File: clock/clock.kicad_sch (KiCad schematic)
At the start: 32 parts

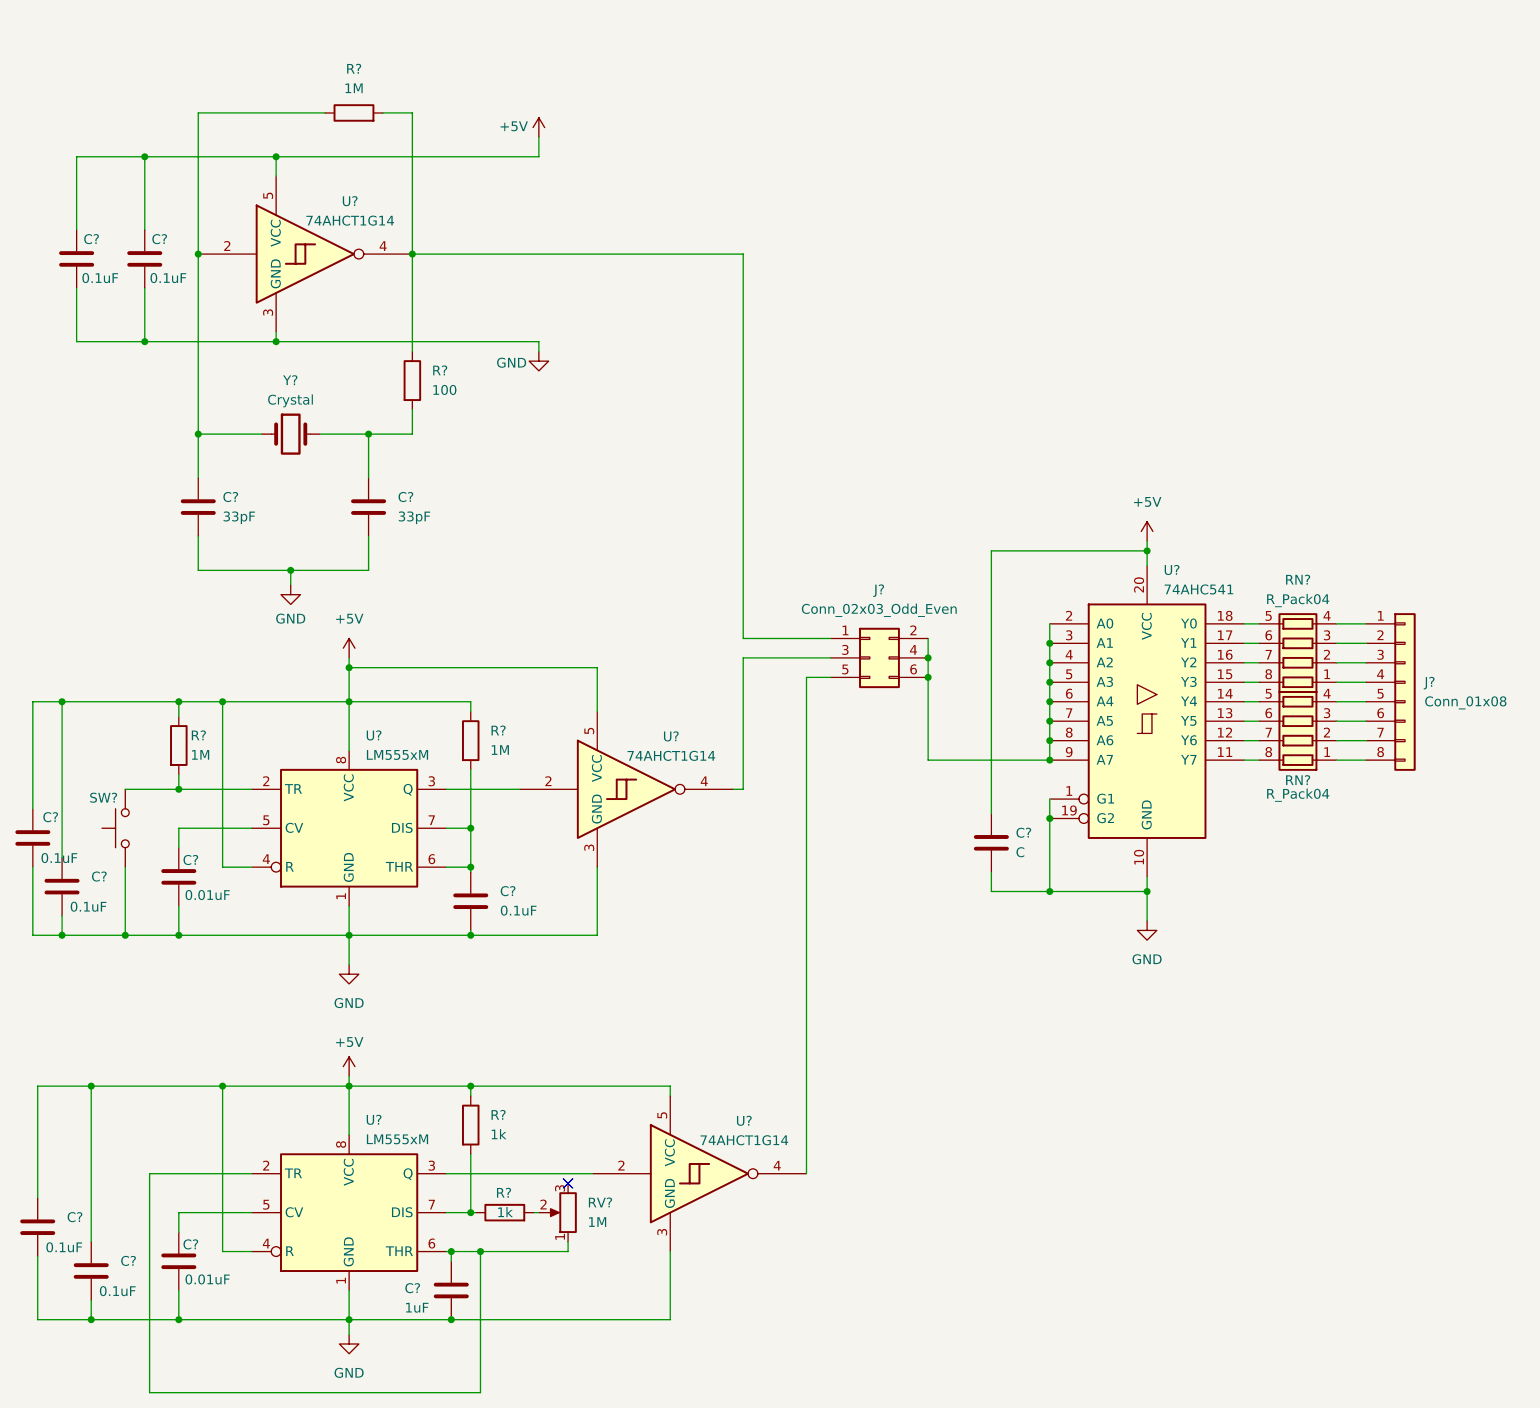
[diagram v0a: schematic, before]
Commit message: Finalized clock for fabrication
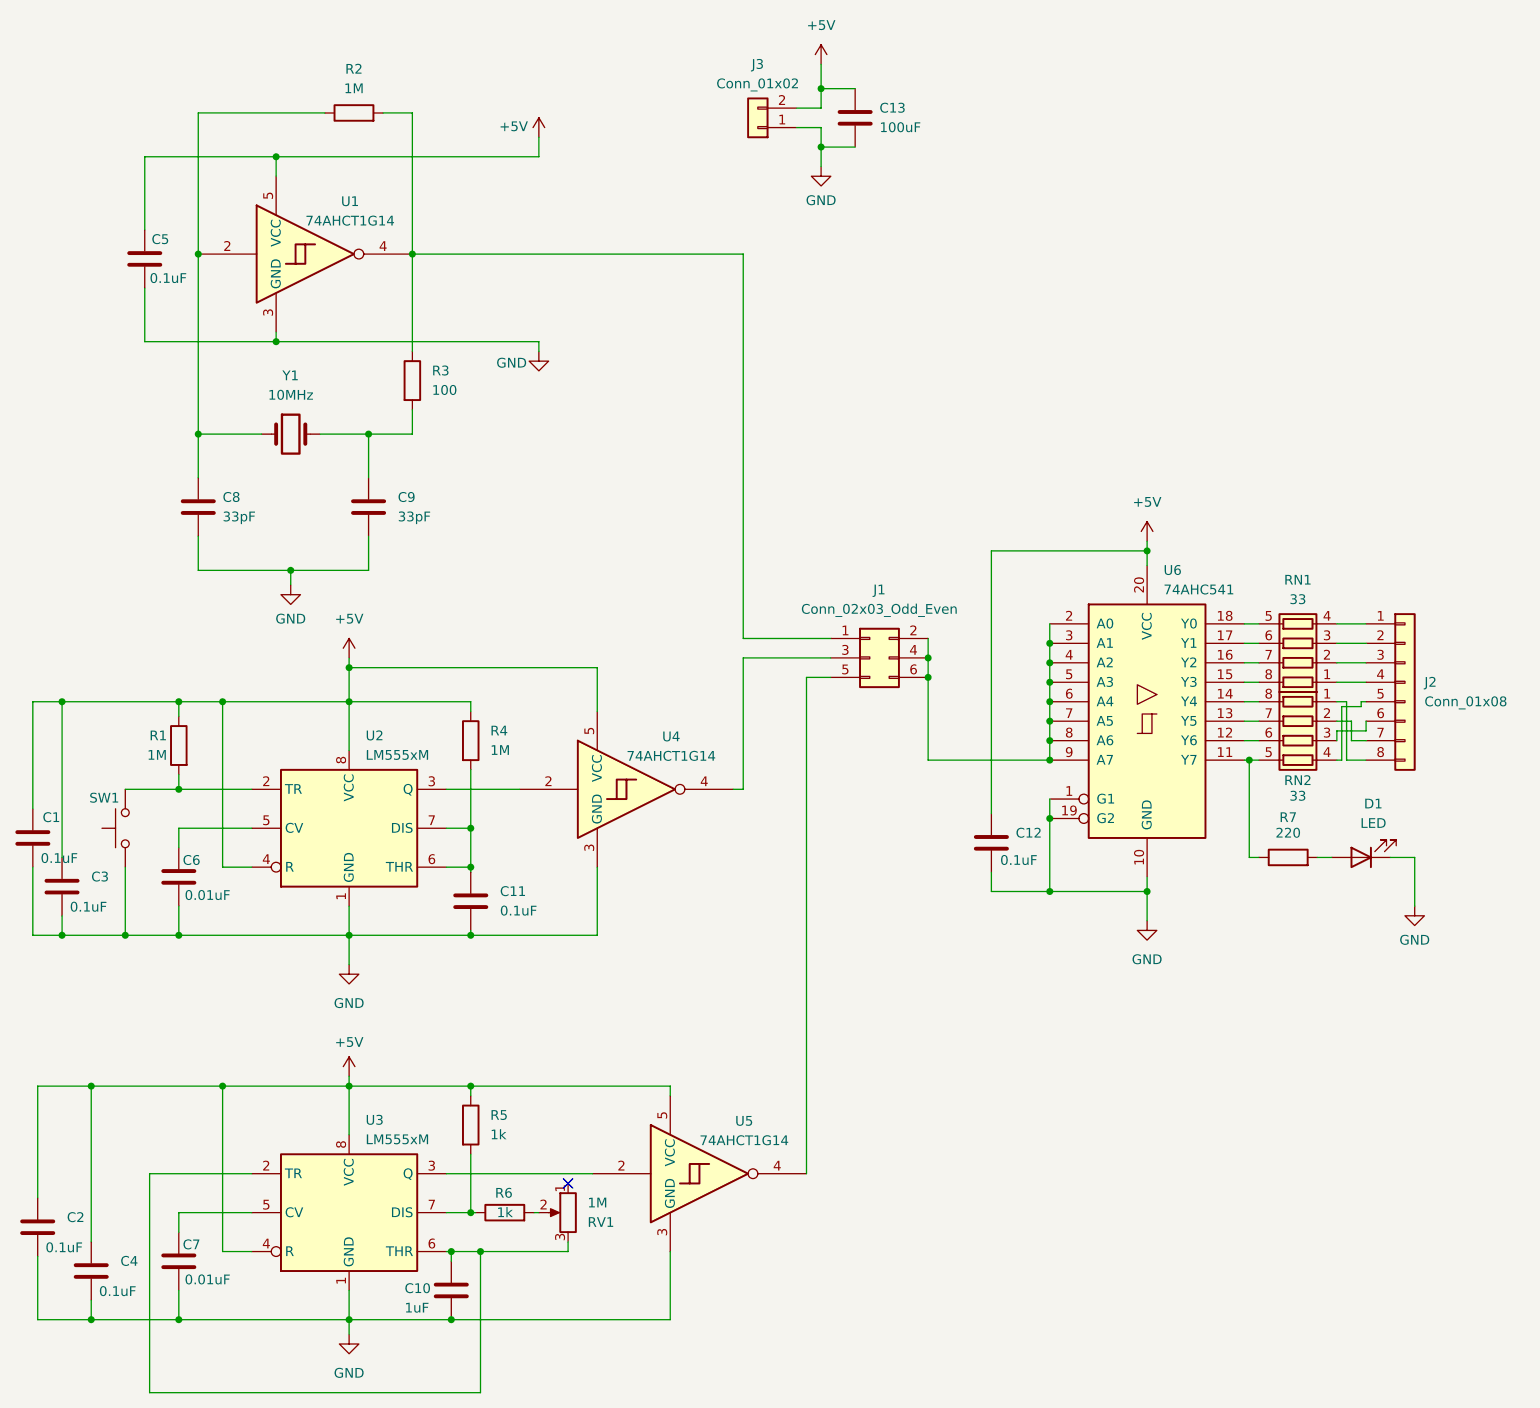
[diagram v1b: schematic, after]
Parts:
- removed C?: 0.1uF, symbol Device:C
- added C13: 100uF, Capacitor_SMD:CP_Elec_5x5.3, symbol Device:C
- added D1: LED, LED_SMD:LED_0603_1608Metric, symbol Device:LED
- added J3: Conn_01x02, Connector_PinHeader_2.54mm:PinHeader_1x02_P2.54mm_Vertical, symbol Connector_Generic:Conn_01x02
- added R7: 220, Resistor_SMD:R_0603_1608Metric, symbol Device:R
- C1, C10, C11, C2, C3, C4, C5, C6, C7, C8, C9: renamed from C?; footprint (none) -> Capacitor_SMD:C_0603_1608Metric
- C12: renamed from C?; value C -> 0.1uF; footprint (none) -> Capacitor_SMD:C_0603_1608Metric
- J1: renamed from J?; footprint (none) -> Connector_PinHeader_2.54mm:PinHeader_2x03_P2.54mm_Vertical
- J2: renamed from J?; footprint (none) -> Connector_PinHeader_2.54mm:PinHeader_1x08_P2.54mm_Vertical
- R1, R2, R3, R4, R5, R6: renamed from R?; footprint (none) -> Resistor_SMD:R_0603_1608Metric
- RN1, RN2: renamed from RN?; value R_Pack04 -> 33; footprint (none) -> Resistor_SMD:R_Array_Convex_4x1206
- RV1: renamed from RV?; footprint (none) -> Potentiometer_THT:Potentiometer_Piher_PT-6-V_Vertical
- SW1: renamed from SW?; footprint (none) -> Button_Switch_THT:SW_PUSH_6mm
- U1, U4, U5: renamed from U?; footprint (none) -> Package_TO_SOT_SMD:SOT-23-5
- U6: renamed from U?; footprint (none) -> Package_SO:TSSOP-20_4.4x6.5mm_P0.65mm
- Y1: renamed from Y?; value Crystal -> 10MHz; footprint (none) -> Crystal:Crystal_HC49-U_Vertical
- gave numbers to parts that had none: 2
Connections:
- net +5V: now also C13.1, J3.2 (Pin_2)
- net GND: now also C13.2, D1.1 (K), J3.1 (Pin_1)
- net at RN2.5 (R4.2): now also U6.11 (Y7), R7.1; no longer U6.14 (Y4)
- net at RN2.6 (R3.2): now also U6.12 (Y6); no longer U6.13 (Y5)
- net at RN2.7 (R2.2): now also U6.13 (Y5); no longer U6.12 (Y6)
- net at RN2.8 (R1.2): now also U6.14 (Y4); no longer U6.11 (Y7)
- net at C10.1, U3.2 (TR), U3.6 (THR): now also RV1.3; no longer RV1.1
- new net: D1.2 (A), R7.2
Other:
- moved on the sheet: RV1
